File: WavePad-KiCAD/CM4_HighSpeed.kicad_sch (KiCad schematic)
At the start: 5 parts, among them J15 Conn_01x22_Female, J6 THD-02-R

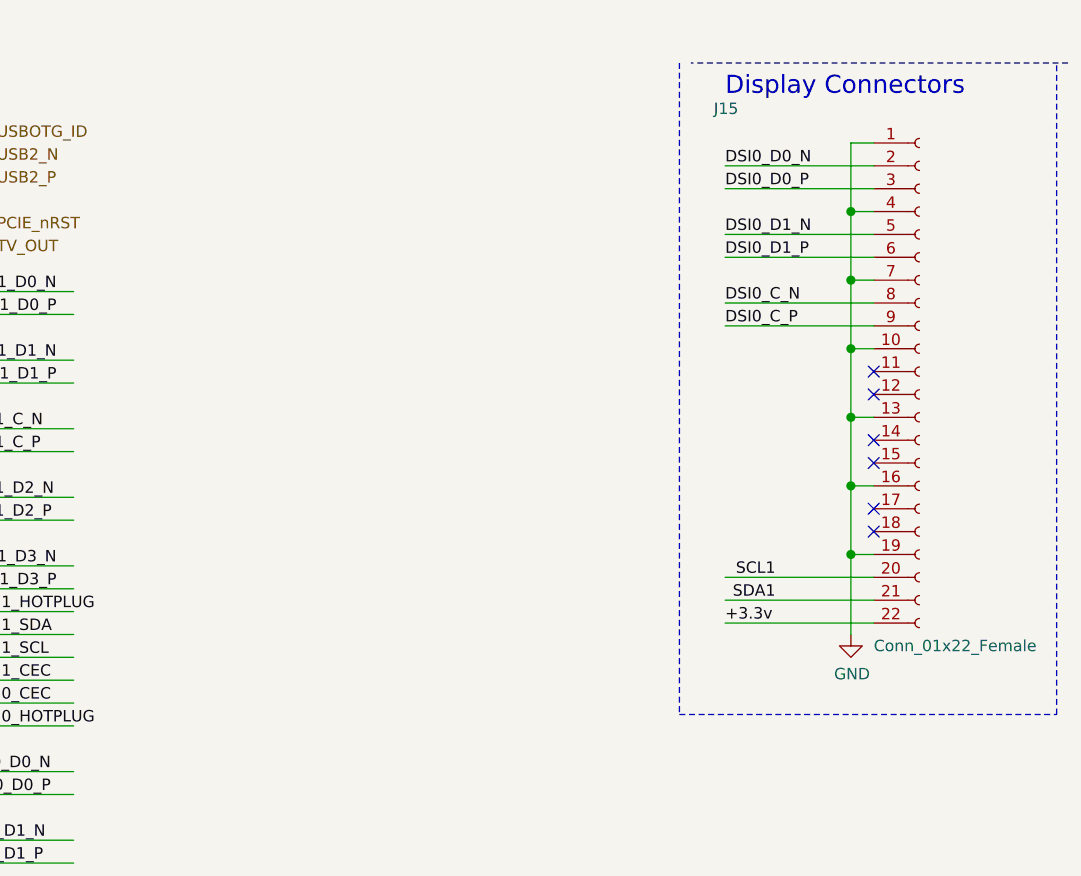
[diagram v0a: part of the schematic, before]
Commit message: Started PCB
Added CSI and DSI connector as well as a USB C with protected  data and Power
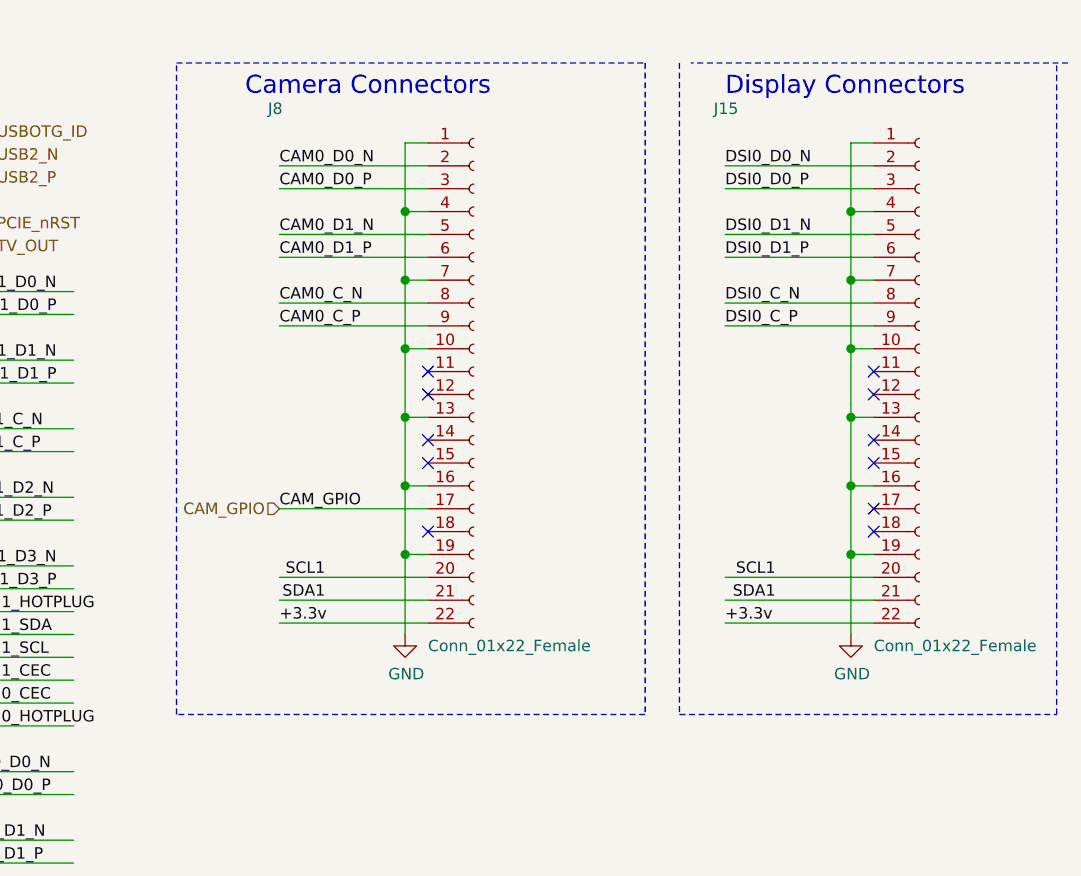
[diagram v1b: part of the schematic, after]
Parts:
- added J8: Conn_01x22_Female, CM4IO:Hirose_FH12-22S-0.5SH_1x22-1MP_P0.50mm_Horizontal, symbol Connector:Conn_01x22_Female
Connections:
- net +3.3v: now also J8.22 (Pin_22)
- net CAM0_C_N: now also J8.8 (Pin_8)
- net CAM0_C_P: now also J8.9 (Pin_9)
- net CAM0_D0_N: now also J8.2 (Pin_2)
- net CAM0_D0_P: now also J8.3 (Pin_3)
- net CAM0_D1_N: now also J8.5 (Pin_5)
- net CAM0_D1_P: now also J8.6 (Pin_6)
- net GND: now also J8.1 (Pin_1), J8.10 (Pin_10), J8.13 (Pin_13), J8.16 (Pin_16), J8.19 (Pin_19), J8.4 (Pin_4), J8.7 (Pin_7)
- net SCL1: now also J8.20 (Pin_20)
- net SDA1: now also J8.21 (Pin_21)
- new net CAM_GPIO: J8.17 (Pin_17)
- no-connect marks 8 -> 13
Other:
- note added: "Camera Connectors"

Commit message: Worked on PCB
Almost finished the PCB
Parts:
- removed J6: THD-02-R, Connector_PinHeader_2.54mm:PinHeader_2x02_P2.54mm_Vertical, symbol Connector_Generic:Conn_02x02_Odd_Even
- removed R6, R7: 2.2K 1%, Resistor_SMD:R_0402_1005Metric, symbol Device:R
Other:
- note removed: "Jumpers to be fitted if Camera0 or Display0 are used."
